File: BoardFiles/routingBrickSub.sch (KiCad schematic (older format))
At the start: 1 part

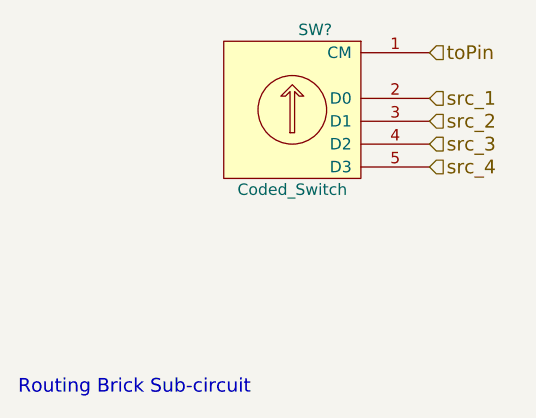
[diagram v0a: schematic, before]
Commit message: Created ComponentBrick.pro
Created Component Brick Project.  Added component library for MdSDE,
included relative search path, included library.
Added schematic component for DIP Switches “SPST_x3”
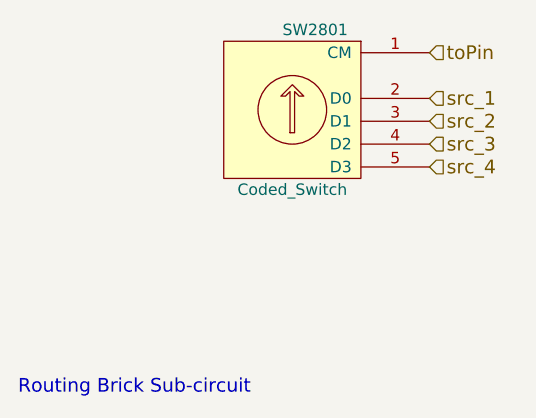
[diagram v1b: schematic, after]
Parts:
- gave numbers to parts that had none: 1
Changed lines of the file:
@@
 $EndDescr
 $Comp
-L Coded_Switch SW?
+L Coded_Switch SW1301
 U 1 1 56A68E41
 P 4500 2850
-F 0 "SW?" H 4600 3200 50  0000 C CNN
+AR Path="/56A65E96/56A68C1E/56A68E41" Ref="SW1301"  Part="1"
+AR Path="/56A65E96/56A76DB9/56A68E41" Ref="SW1401"  Part="1"
+AR Path="/56A65E96/56A77620/56A68E41" Ref="SW1501"  Part="1"
+AR Path="/56A65E96/56A77636/56A68E41" Ref="SW1601"  Part="1"
+AR Path="/56A65E96/56A77F9B/56A68E41" Ref="SW1701"  Part="1"
+AR Path="/56A65E96/56A77FB1/56A68E41" Ref="SW1801"  Part="1"
+AR Path="/56A65E96/56A77FC7/56A68E41" Ref="SW1901"  Part="1"
+AR Path="/56A65E96/56A77FDD/56A68E41" Ref="SW2001"  Part="1"
+AR Path="/56A65E96/56A7A9FE/56A68E41" Ref="SW2101"  Part="1"
+AR Path="/56A65E96/56A7AA14/56A68E41" Ref="SW2201"  Part="1"
+AR Path="/56A65E96/56A7AA2A/56A68E41" Ref="SW2301"  Part="1"
+AR Path="/56A65E96/56A7AA40/56A68E41" Ref="SW2401"  Part="1"
+AR Path="/56A65E96/56A7AA56/56A68E41" Ref="SW2501"  Part="1"
+AR Path="/56A65E96/56A7AA6C/56A68E41" Ref="SW2601"  Part="1"
+AR Path="/56A65E96/56A7AA82/56A68E41" Ref="SW2701"  Part="1"
+AR Path="/56A65E96/56A7AA98/56A68E41" Ref="SW2801"  Part="1"
+F 0 "SW2801" H 4600 3200 50  0000 C CNN
 F 1 "Coded_Switch" H 4500 2501 50  0000 C CNN
 F 2 "" H 4500 2850 60  0000 C CNN
